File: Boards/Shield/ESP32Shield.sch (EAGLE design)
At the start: 27 parts, among them Q1 220mA/50V/3.5Ω, U1 5V

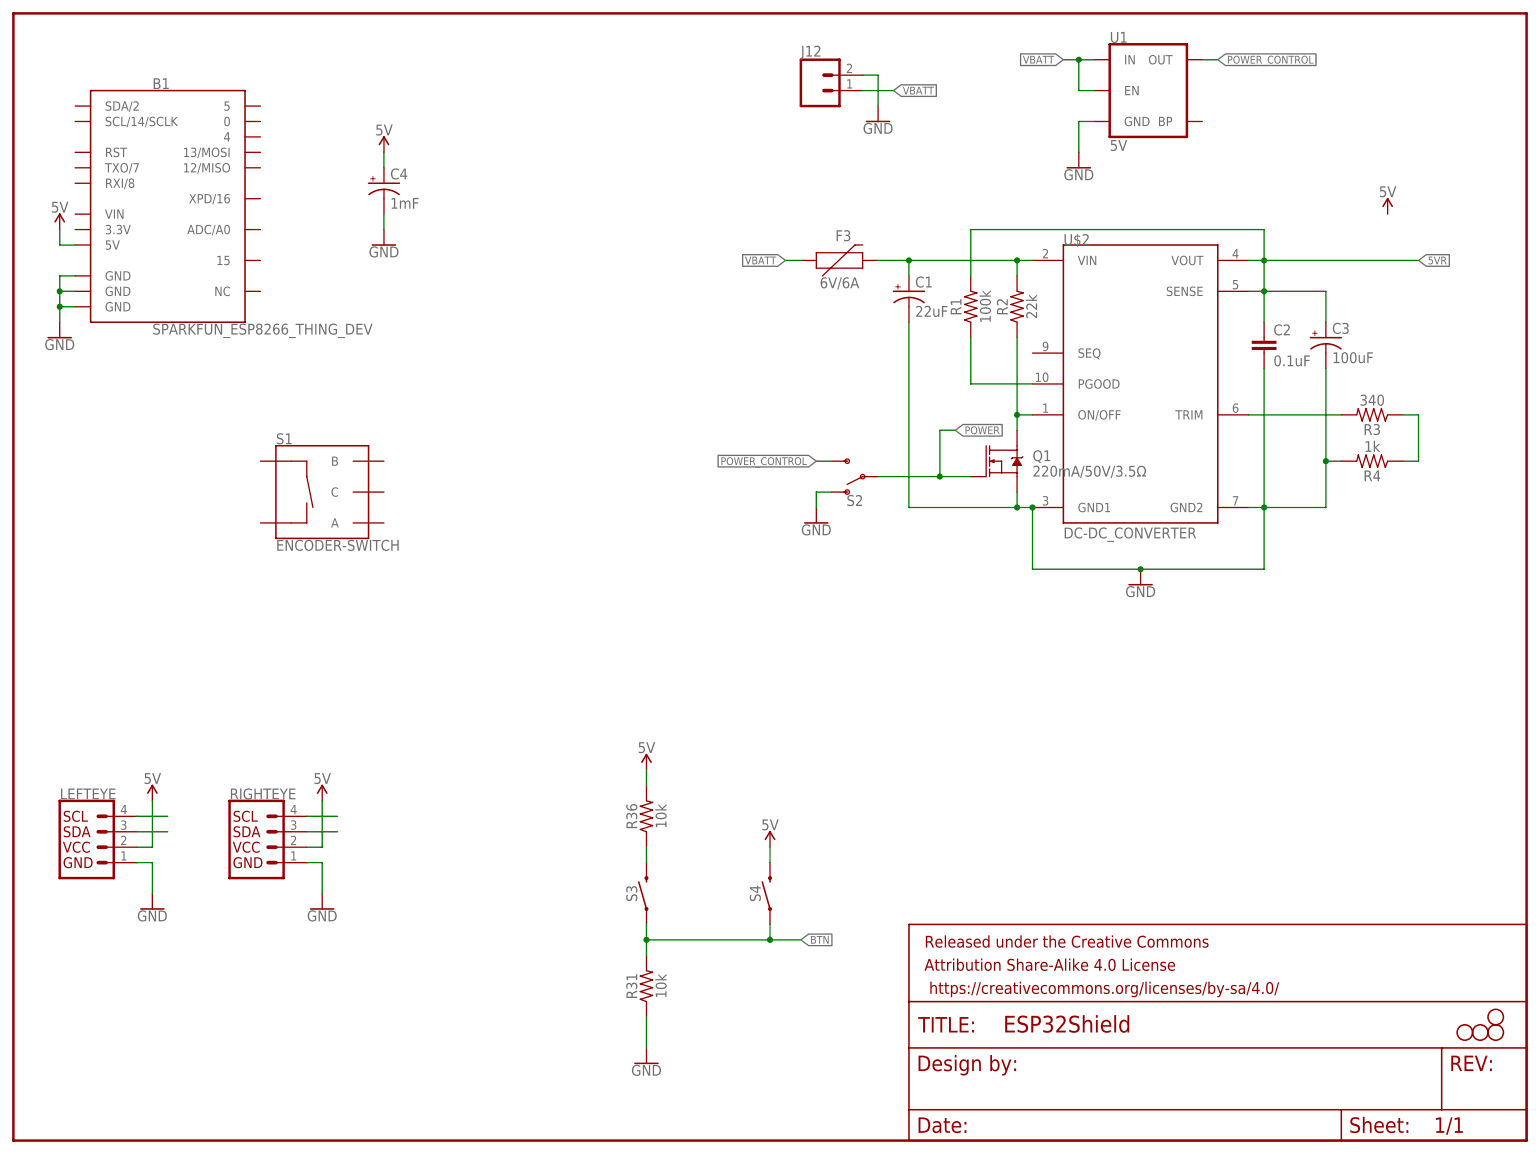
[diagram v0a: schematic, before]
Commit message: Laid out ESP32 Shield
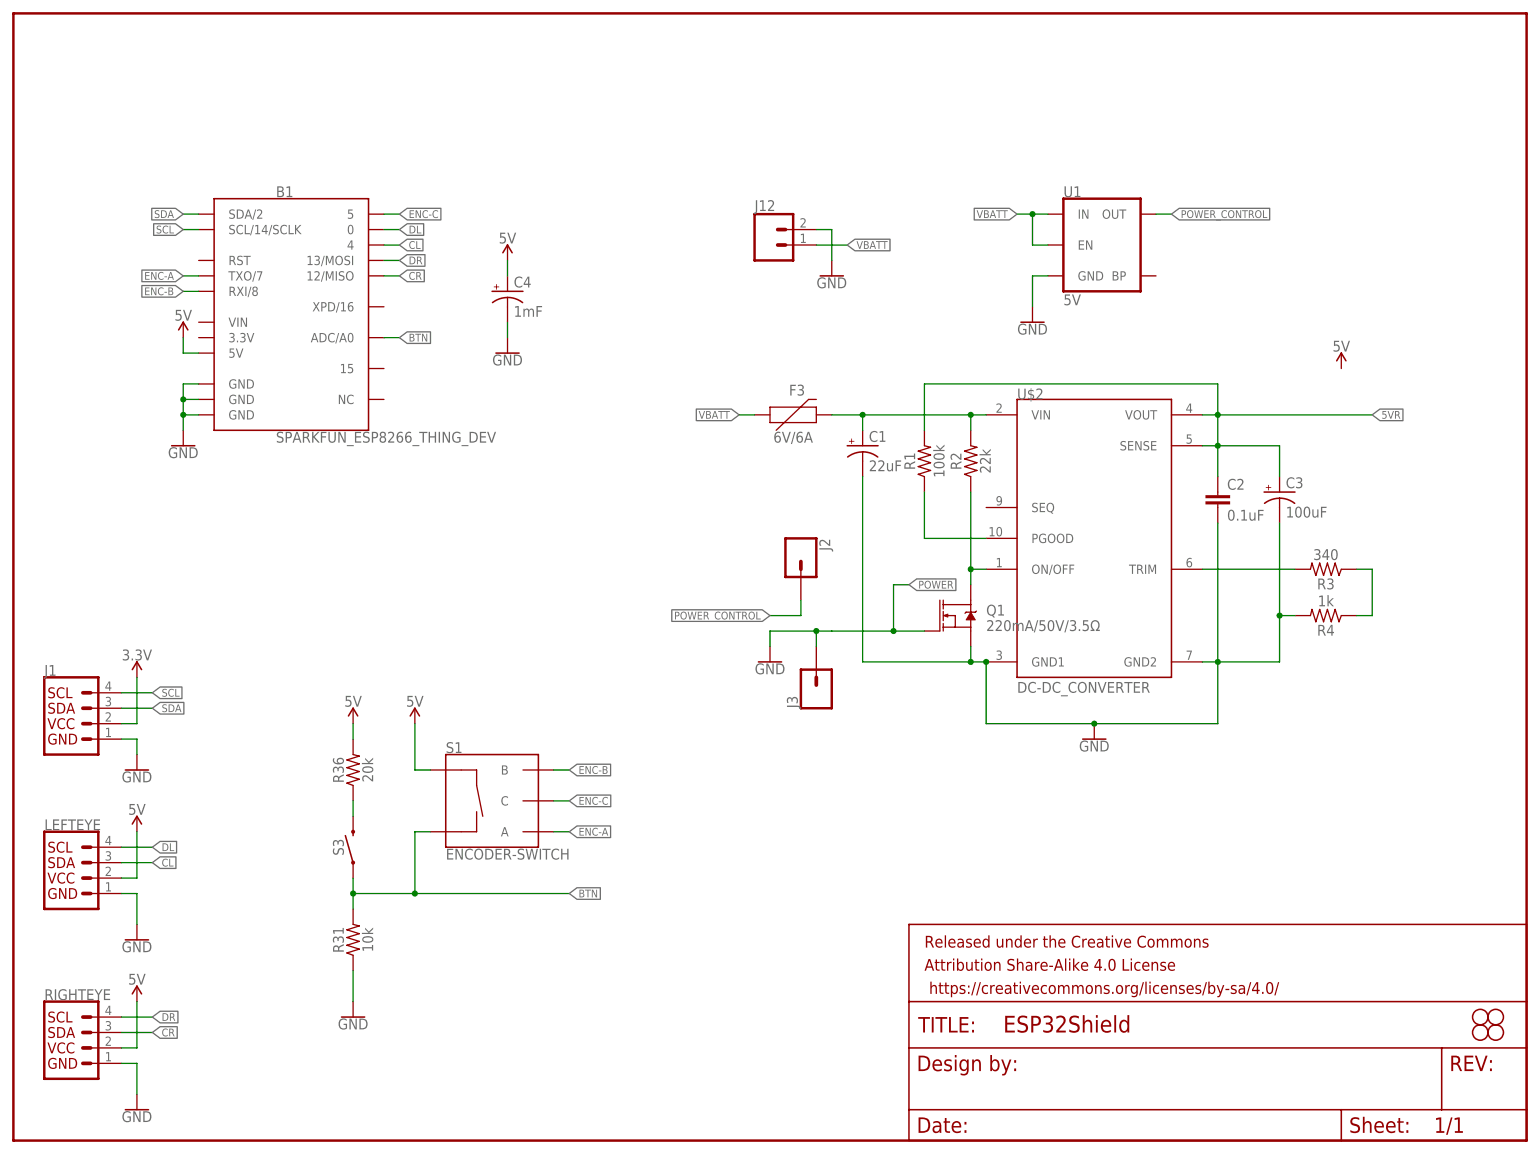
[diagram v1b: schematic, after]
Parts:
- removed S2: (no value), SparkFun-Switches:SWITCH-SPDT-SMD-RIGHT-ANGLE
- removed S4: MOMENTARY-SWITCH-SPST-PTH-RIGHT-ANGLE-KIT, SparkFun-Switches:MOMENTARY-SWITCH-SPST-PTH-RIGHT-ANGLE-KIT
- added J1: (no value), SparkFun-Connectors:QWIIC_CONNECTORJS-1MM
- added J2, J3: (no value), SparkFun-Connectors:CONN_01
- R36: value 10k -> 20k; device SparkFun-Resistors:10KOHM-0603-1/10W-1% -> SparkFun-Resistors:20KOHM-0603-1/10W-5%
- S3: value MOMENTARY-SWITCH-SPST-PTH-RIGHT-ANGLE-KIT -> MOMENTARY-SWITCH-SPST-SMD-4.5MM; device SparkFun-Switches:MOMENTARY-SWITCH-SPST-PTH-RIGHT-ANGLE-KIT -> SparkFun-Switches:MOMENTARY-SWITCH-SPST-SMD-4.5MM
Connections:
- removed net N$1: LEFTEYE.4
- removed net N$6: LEFTEYE.3
- removed net N$7: RIGHTEYE.4
- removed net N$8: RIGHTEYE.3
- new net 3.3V: J1.2
- new net CL: B1.4, LEFTEYE.3
- new net CR: B1.12/MISO, RIGHTEYE.3
- new net DL: B1.0, LEFTEYE.4
- new net DR: B1.13/MOSI, RIGHTEYE.4
- new net ENC-A: B1.TXO/7, S1.A
- new net ENC-B: B1.RXI/8, S1.B
- new net ENC-C: B1.5, S1.C
- new net SCL: B1.SCL/14/SCLK, J1.4
- new net SDA: B1.SDA/2, J1.3
- net 5V: now also S1.SW+; no longer S4.2
- net BTN: now also B1.ADC/A0, S1.SW-; no longer S4.1
- net GND: now also J1.1, J3.1; no longer S2.O
- net POWER: no longer S2.P
- net POWER_CONTROL: now also J2.1; no longer S2.S
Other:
- moved on the sheet: B1, C1, C2, C3, C4, F3, J12, LEFTEYE, Q1, R1, R2, R3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

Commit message: began layout
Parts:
- added J4: (no value), SparkFun-Connectors:CONN_01
- LEFTEYE, RIGHTEYE: device SparkFun-Connectors:QWIIC_CONNECTORJS-1MM -> SparkFun-Connectors:CONN_04
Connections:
- removed net 5VR: C2.1, C3.+, R1.2, U$2.SENSE, U$2.VOUT
- removed net POWER: Q1.G
- net 3.3V: now also B1.3.3V
- net 5V: now also C2.1, C3.+, J4.1, R1.2, U$2.SENSE, U$2.VOUT
- net GND: now also Q1.G
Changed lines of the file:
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@@
 <part name="FRAME1" library="SparkFun-Aesthetics" deviceset="FRAME-LETTER" device=""/>
 <part name="J12" library="SparkFun-Connectors" deviceset="CONN_02" device="5MM"/>
-<part name="LEFTEYE" library="SparkFun-Connectors" deviceset="QWIIC_CONNECTOR" device="JS-1MM"/>
+<part name="LEFTEYE" library="SparkFun-Connectors" deviceset="CONN_04" device=""/>
 <part name="GND15" library="SparkFun-PowerSymbols" deviceset="GND" device=""/>
-<part name="RIGHTEYE" library="SparkFun-Connectors" deviceset="QWIIC_CONNECTOR" device="JS-1MM"/>
+<part name="RIGHTEYE" library="SparkFun-Connectors" deviceset="CONN_04" device=""/>
 <part name="GND17" library="SparkFun-PowerSymbols" deviceset="GND" device=""/>
 <part name="R31" library="SparkFun-Resistors" deviceset="10KOHM" device="-0603-1/10W-1%" value="10k"/>
@@
 <part name="J2" library="SparkFun-Connectors" deviceset="CONN_01" device=""/>
 <part name="J3" library="SparkFun-Connectors" deviceset="CONN_01" device=""/>
+<part name="SUPPLY6" library="SparkFun-PowerSymbols" deviceset="3.3V" device=""/>
+<part name="J4" library="SparkFun-Connectors" deviceset="CONN_01" device=""/>
 </parts>
 <sheets>
@@
 <instance part="SUPPLY4" gate="G$1" x="20.32" y="50.8"/>
 <instance part="SUPPLY5" gate="G$1" x="55.88" y="68.58"/>
-<instance part="SUPPLY7" gate="G$1" x="27.94" y="132.08"/>
+<instance part="SUPPLY7" gate="G$1" x="25.4" y="132.08"/>
 <instance part="S1" gate="G$1" x="78.74" y="55.88"/>
 <instance part="J1" gate="G$1" x="10.16" y="68.58"/>
@@
 <instance part="J2" gate="G$1" x="129.54" y="96.52" rot="R270"/>
 <instance part="J3" gate="G$1" x="132.08" y="73.66" rot="R90"/>
+<instance part="SUPPLY6" gate="G$1" x="27.94" y="134.62"/>
+<instance part="J4" gate="G$1" x="15.24" y="129.54"/>
 </instances>
 <busses>
@@
 <segment>
 <pinref part="LEFTEYE" gate="G$1" pin="1"/>
-<wire x1="17.78" y1="40.64" x2="20.32" y2="40.64" width="0.1524" layer="91"/>
+<wire x1="15.24" y1="40.64" x2="20.32" y2="40.64" width="0.1524" layer="91"/>
 <wire x1="20.32" y1="40.64" x2="20.32" y2="35.56" width="0.1524" layer="91"/>
 <pinref part="GND15" gate="1" pin="GND"/>
@@
 <segment>
 <pinref part="RIGHTEYE" gate="G$1" pin="1"/>
-<wire x1="17.78" y1="12.7" x2="20.32" y2="12.7" width="0.1524" layer="91"/>
+<wire x1="15.24" y1="12.7" x2="20.32" y2="12.7" width="0.1524" layer="91"/>
 <wire x1="20.32" y1="12.7" x2="20.32" y2="7.62" width="0.1524" layer="91"/>
 <pinref part="GND17" gate="1" pin="GND"/>
@@
 <wire x1="124.46" y1="83.82" x2="132.08" y2="83.82" width="0.1524" layer="91"/>
 <pinref part="J3" gate="G$1" pin="1"/>
-<wire x1="132.08" y1="83.82" x2="134.62" y2="83.82" width="0.1524" layer="91"/>
 <wire x1="132.08" y1="81.28" x2="132.08" y2="83.82" width="0.1524" layer="91"/>
+<pinref part="Q1" gate="NMOS" pin="G"/>
+<wire x1="149.86" y1="83.82" x2="132.08" y2="83.82" width="0.1524" layer="91"/>
 <junction x="132.08" y="83.82"/>
 </segment>
@@
 </segment>
 </net>
-<net name="5VR" class="0">
-<segment>
-<pinref part="U$2" gate="G$1" pin="VOUT"/>
-<wire x1="195.58" y1="119.38" x2="198.12" y2="119.38" width="0.1524" layer="91"/>
-<wire x1="198.12" y1="119.38" x2="223.52" y2="119.38" width="0.1524" layer="91"/>
-<pinref part="U$2" gate="G$1" pin="SENSE"/>
-<wire x1="195.58" y1="114.3" x2="198.12" y2="114.3" width="0.1524" layer="91"/>
-<wire x1="198.12" y1="119.38" x2="198.12" y2="114.3" width="0.1524" layer="91"/>
-<junction x="198.12" y="119.38"/>
-<label x="223.52" y="119.38" size="1.27" layer="95" font="vector" ratio="15" xref="yes"/>
-<pinref part="C2" gate="G$1" pin="1"/>
-<wire x1="198.12" y1="114.3" x2="198.12" y2="109.22" width="0.1524" layer="91"/>
-<junction x="198.12" y="114.3"/>
-<pinref part="C3" gate="G$1" pin="+"/>
-<wire x1="198.12" y1="114.3" x2="208.28" y2="114.3" width="0.1524" layer="91"/>
-<wire x1="208.28" y1="114.3" x2="208.28" y2="109.22" width="0.1524" layer="91"/>
-<pinref part="R1" gate="G$1" pin="2"/>
-<wire x1="149.86" y1="116.84" x2="149.86" y2="124.46" width="0.1524" layer="91"/>
-<wire x1="149.86" y1="124.46" x2="198.12" y2="124.46" width="0.1524" layer="91"/>
-<wire x1="198.12" y1="124.46" x2="198.12" y2="119.38" width="0.1524" layer="91"/>
-</segment>
-</net>
-<net name="POWER" class="0">
-<segment>
-<pinref part="Q1" gate="NMOS" pin="G"/>
-<wire x1="134.62" y1="83.82" x2="144.78" y2="83.82" width="0.1524" layer="91"/>
-<wire x1="144.78" y1="83.82" x2="149.86" y2="83.82" width="0.1524" layer="91"/>
-<wire x1="144.78" y1="83.82" x2="144.78" y2="91.44" width="0.1524" layer="91"/>
-<junction x="144.78" y="83.82"/>
-<wire x1="144.78" y1="91.44" x2="147.32" y2="91.44" width="0.1524" layer="91"/>
-<label x="147.32" y="91.44" size="1.27" layer="95" xref="yes"/>
-</segment>
-</net>
 <net name="N$2" class="0">
 <segment>
@@
 <segment>
 <pinref part="RIGHTEYE" gate="G$1" pin="2"/>
-<wire x1="17.78" y1="15.24" x2="20.32" y2="15.24" width="0.1524" layer="91"/>
+<wire x1="15.24" y1="15.24" x2="20.32" y2="15.24" width="0.1524" layer="91"/>
 <wire x1="20.32" y1="15.24" x2="20.32" y2="22.86" width="0.1524" layer="91"/>
 <pinref part="SUPPLY3" gate="G$1" pin="5V"/>
@@
 <segment>
 <pinref part="LEFTEYE" gate="G$1" pin="2"/>
-<wire x1="17.78" y1="43.18" x2="20.32" y2="43.18" width="0.1524" layer="91"/>
+<wire x1="15.24" y1="43.18" x2="20.32" y2="43.18" width="0.1524" layer="91"/>
 <wire x1="20.32" y1="43.18" x2="20.32" y2="50.8" width="0.1524" layer="91"/>
 <pinref part="SUPPLY4" gate="G$1" pin="5V"/>
@@
 <pinref part="SUPPLY7" gate="G$1" pin="5V"/>
 <pinref part="B1" gate="G$1" pin="5V"/>
-<wire x1="27.94" y1="132.08" x2="27.94" y2="129.54" width="0.1524" layer="91"/>
-<wire x1="27.94" y1="129.54" x2="30.48" y2="129.54" width="0.1524" layer="91"/>
+<wire x1="25.4" y1="132.08" x2="25.4" y2="129.54" width="0.1524" layer="91"/>
+<wire x1="25.4" y1="129.54" x2="30.48" y2="129.54" width="0.1524" layer="91"/>
+<pinref part="J4" gate="G$1" pin="1"/>
+<wire x1="25.4" y1="129.54" x2="22.86" y2="129.54" width="0.1524" layer="91"/>
+<junction x="25.4" y="129.54"/>
 </segment>
 <segment>
@@
 <wire x1="66.04" y1="60.96" x2="66.04" y2="68.58" width="0.1524" layer="91"/>
 </segment>
+<segment>
+<pinref part="U$2" gate="G$1" pin="VOUT"/>
+<wire x1="195.58" y1="119.38" x2="198.12" y2="119.38" width="0.1524" layer="91"/>
+<pinref part="U$2" gate="G$1" pin="SENSE"/>
+<wire x1="195.58" y1="114.3" x2="198.12" y2="114.3" width="0.1524" layer="91"/>
+<wire x1="198.12" y1="119.38" x2="198.12" y2="114.3" width="0.1524" layer="91"/>
+<junction x="198.12" y="119.38"/>
+<pinref part="C2" gate="G$1" pin="1"/>
+<wire x1="198.12" y1="114.3" x2="198.12" y2="109.22" width="0.1524" layer="91"/>
+<junction x="198.12" y="114.3"/>
+<pinref part="C3" gate="G$1" pin="+"/>
+<wire x1="198.12" y1="114.3" x2="208.28" y2="114.3" width="0.1524" layer="91"/>
+<wire x1="208.28" y1="114.3" x2="208.28" y2="109.22" width="0.1524" layer="91"/>
+<pinref part="R1" gate="G$1" pin="2"/>
+<wire x1="149.86" y1="116.84" x2="149.86" y2="124.46" width="0.1524" layer="91"/>
+<wire x1="149.86" y1="124.46" x2="198.12" y2="124.46" width="0.1524" layer="91"/>
+<wire x1="198.12" y1="124.46" x2="198.12" y2="119.38" width="0.1524" layer="91"/>
+<pinref part="SUPPLY2" gate="G$1" pin="5V"/>
+<wire x1="198.12" y1="119.38" x2="218.44" y2="119.38" width="0.1524" layer="91"/>
+<wire x1="218.44" y1="119.38" x2="218.44" y2="127" width="0.1524" layer="91"/>
+</segment>
 </net>
 <net name="SDA" class="0">
@@
 <pinref part="SUPPLY8" gate="G$1" pin="3.3V"/>
 </segment>
+<segment>
+<pinref part="B1" gate="G$1" pin="3.3V"/>
+<wire x1="30.48" y1="132.08" x2="27.94" y2="132.08" width="0.1524" layer="91"/>
+<wire x1="27.94" y1="132.08" x2="27.94" y2="134.62" width="0.1524" layer="91"/>
+<pinref part="SUPPLY6" gate="G$1" pin="3.3V"/>
+</segment>
 </net>
 <net name="DL" class="0">
@@
 <segment>
 <pinref part="LEFTEYE" gate="G$1" pin="4"/>
-<wire x1="17.78" y1="48.26" x2="22.86" y2="48.26" width="0.1524" layer="91"/>
+<wire x1="15.24" y1="48.26" x2="22.86" y2="48.26" width="0.1524" layer="91"/>
 <label x="22.86" y="48.26" size="1.27" layer="95" font="vector" xref="yes"/>
 </segment>
@@
 <segment>
 <pinref part="LEFTEYE" gate="G$1" pin="3"/>
-<wire x1="17.78" y1="45.72" x2="22.86" y2="45.72" width="0.1524" layer="91"/>
+<wire x1="15.24" y1="45.72" x2="22.86" y2="45.72" width="0.1524" layer="91"/>
 <label x="22.86" y="45.72" size="1.27" layer="95" font="vector" xref="yes"/>
 </segment>
@@
 <segment>
 <pinref part="RIGHTEYE" gate="G$1" pin="4"/>
-<wire x1="17.78" y1="20.32" x2="22.86" y2="20.32" width="0.1524" layer="91"/>
+<wire x1="15.24" y1="20.32" x2="22.86" y2="20.32" width="0.1524" layer="91"/>
 <label x="22.86" y="20.32" size="1.27" layer="95" font="vector" xref="yes"/>
 </segment>
@@
 <segment>
 <pinref part="RIGHTEYE" gate="G$1" pin="3"/>
-<wire x1="17.78" y1="17.78" x2="22.86" y2="17.78" width="0.1524" layer="91"/>
+<wire x1="15.24" y1="17.78" x2="22.86" y2="17.78" width="0.1524" layer="91"/>
 <label x="22.86" y="17.78" size="1.27" layer="95" font="vector" xref="yes"/>
 </segment>
@@
 <segment>
 <pinref part="B1" gate="G$1" pin="TXO/7"/>
-<wire x1="30.48" y1="142.24" x2="27.94" y2="142.24" width="0.1524" layer="91"/>
-<label x="27.94" y="142.24" size="1.27" layer="95" font="vector" rot="R180" xref="yes"/>
+<wire x1="30.48" y1="142.24" x2="25.4" y2="142.24" width="0.1524" layer="91"/>
+<label x="25.4" y="142.24" size="1.27" layer="95" font="vector" rot="R180" xref="yes"/>
 </segment>
 </net>
@@
 <segment>
 <pinref part="B1" gate="G$1" pin="RXI/8"/>
-<wire x1="30.48" y1="139.7" x2="27.94" y2="139.7" width="0.1524" layer="91"/>
-<label x="27.94" y="139.7" size="1.27" layer="95" font="vector" rot="R180" xref="yes"/>
-</segment>
-</net>
+<wire x1="30.48" y1="139.7" x2="25.4" y2="139.7" width="0.1524" layer="91"/>
+<label x="25.4" y="139.7" size="1.27" layer="95" font="vector" rot="R180" xref="yes"/>
+</segment>
+</net>
